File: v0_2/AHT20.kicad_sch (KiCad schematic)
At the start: 1 part, among them U1 AHT20

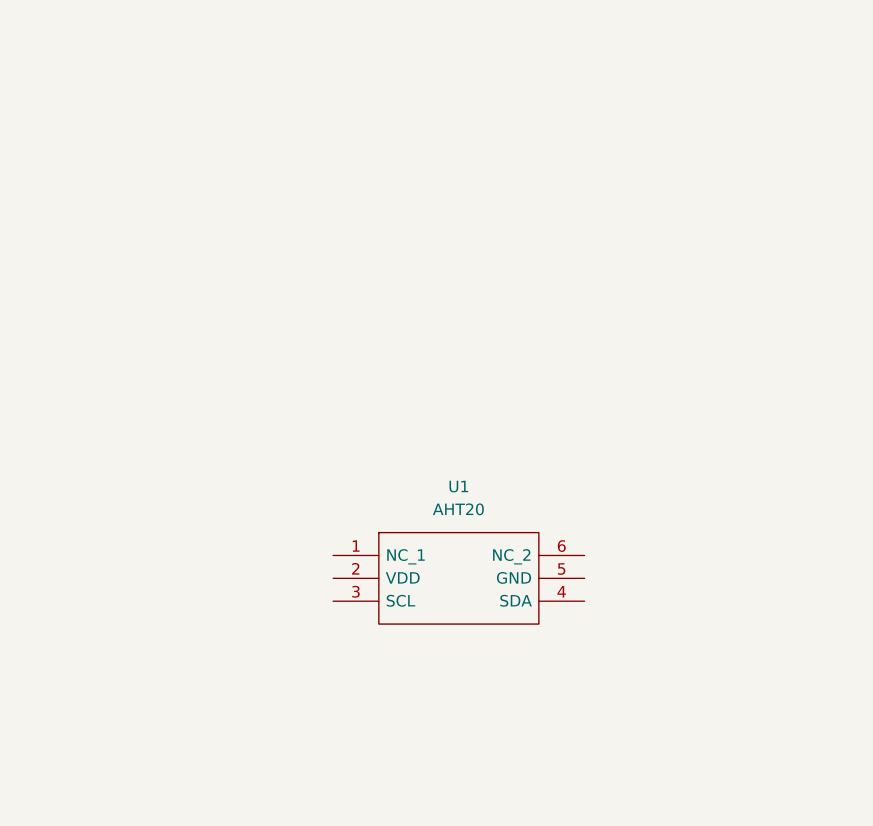
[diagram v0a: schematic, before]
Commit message: add color sensor
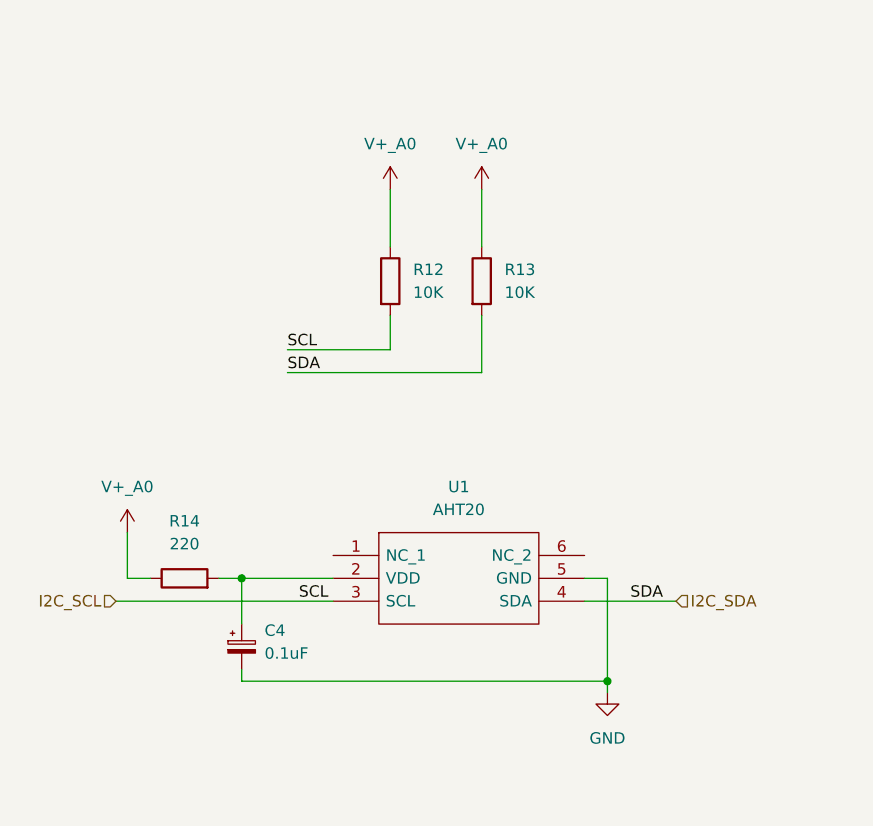
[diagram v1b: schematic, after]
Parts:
- added C4: 0.1uF, symbol Device:C_Polarized_Small
- added R12, R13: 10K, symbol Device:R
- added R14: 220, symbol Device:R
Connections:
- net at U1.2 (VDD): now also C4.1, R14.2
- net I2C_SCL: now reaches U1.3 (SCL)
- net I2C_SCL: now also R12.2
- net I2C_SDA: now reaches U1.4 (SDA)
- net I2C_SDA: now also R13.2
- net GND: now reaches U1.5 (GND)
- net GND: now also C4.2
- new net V+_A0: R12.1, R13.1, R14.1

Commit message: schematic for enviro done
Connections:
- net V+_A0 renamed +3.3V
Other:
- note added: "Temperature / Humidity Sensor"
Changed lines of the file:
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@@
     (stroke (width 0) (type default))
+  )
+  (text "Temperature / Humidity Sensor" (at 93.98 36.83 0)
+    (effects (font (face "Ubuntu") (size 3 3) (thickness 1) bold) (justify left bottom))
   )
   (label "SDA" (at 119.38 71.12 0) (fields_autoplaced)
@@
     )
   )
+  (symbol (lib_id "power:+3.3V") (at 130.81 50.8 0) (unit 1)
+    (in_bom yes) (on_board yes) (dnp no) (fields_autoplaced)
+    (property "Reference" "#PWR018" (at 130.81 54.61 0)
+      (effects (font (size 1.27 1.27)) hide)
+    )
+    (property "Value" "+3.3V" (at 130.81 45.72 0)
+      (effects (font (size 1.27 1.27)))
+    )
+    (property "Footprint" "" (at 130.81 50.8 0)
+      (effects (font (size 1.27 1.27)) hide)
+    )
+    (property "Datasheet" "" (at 130.81 50.8 0)
+      (effects (font (size 1.27 1.27)) hide)
+    )
+    (pin "1")
+    (instances
+      (project "v0_2"
+        (path "/678523e5-508b-4706-b0e0-f17e466a8d09/d7c57ea3-e552-44a2-b229-9294e72b57c9"
+          (reference "#PWR018") (unit 1)
+        )
+      )
+    )
+  )
+  (symbol (lib_id "power:+3.3V") (at 101.6 88.9 0) (unit 1)
+    (in_bom yes) (on_board yes) (dnp no) (fields_autoplaced)
+    (property "Reference" "#PWR022" (at 101.6 92.71 0)
+      (effects (font (size 1.27 1.27)) hide)
+    )
+    (property "Value" "+3.3V" (at 101.6 83.82 0)
+      (effects (font (size 1.27 1.27)))
+    )
+    (property "Footprint" "" (at 101.6 88.9 0)
+      (effects (font (size 1.27 1.27)) hide)
+    )
+    (property "Datasheet" "" (at 101.6 88.9 0)
+      (effects (font (size 1.27 1.27)) hide)
+    )
+    (pin "1")
+    (instances
+      (project "v0_2"
+        (path "/678523e5-508b-4706-b0e0-f17e466a8d09/d7c57ea3-e552-44a2-b229-9294e72b57c9"
+          (reference "#PWR022") (unit 1)
+        )
+      )
+    )
+  )
   (symbol (lib_id "Device:R") (at 130.81 60.96 0) (unit 1)
     (in_bom yes) (on_board yes) (dnp no) (fields_autoplaced)
@@
         (path "/678523e5-508b-4706-b0e0-f17e466a8d09/d7c57ea3-e552-44a2-b229-9294e72b57c9"
           (reference "R12") (unit 1)
-        )
-      )
-    )
-  )
-  (symbol (lib_id "power_vsys:V+_A0") (at 130.81 50.8 0) (unit 1)
-    (in_bom yes) (on_board yes) (dnp no) (fields_autoplaced)
-    (property "Reference" "#PWR09" (at 130.81 54.61 0)
-      (effects (font (size 1.27 1.27)) hide)
-    )
-    (property "Value" "V+_A0" (at 130.81 45.72 0)
-      (effects (font (size 1.27 1.27)))
-    )
-    (property "Footprint" "" (at 130.81 50.8 0)
-      (effects (font (size 1.27 1.27)) hide)
-    )
-    (property "Datasheet" "" (at 130.81 50.8 0)
-      (effects (font (size 1.27 1.27)) hide)
-    )
-    (pin "1")
-    (instances
-      (project "v0_2"
-        (path "/678523e5-508b-4706-b0e0-f17e466a8d09"
-          (reference "#PWR09") (unit 1)
-        )
-        (path "/678523e5-508b-4706-b0e0-f17e466a8d09/d7c57ea3-e552-44a2-b229-9294e72b57c9"
-          (reference "#PWR018") (unit 1)
         )
       )
@@
     )
   )
-  (symbol (lib_id "power_vsys:V+_A0") (at 140.97 50.8 0) (unit 1)
-    (in_bom yes) (on_board yes) (dnp no) (fields_autoplaced)
-    (property "Reference" "#PWR09" (at 140.97 54.61 0)
-      (effects (font (size 1.27 1.27)) hide)
-    )
-    (property "Value" "V+_A0" (at 140.97 45.72 0)
+  (symbol (lib_id "power:+3.3V") (at 140.97 50.8 0) (unit 1)
+    (in_bom yes) (on_board yes) (dnp no) (fields_autoplaced)
+    (property "Reference" "#PWR019" (at 140.97 54.61 0)
+      (effects (font (size 1.27 1.27)) hide)
+    )
+    (property "Value" "+3.3V" (at 140.97 45.72 0)
       (effects (font (size 1.27 1.27)))
     )
@@
     (instances
       (project "v0_2"
-        (path "/678523e5-508b-4706-b0e0-f17e466a8d09"
-          (reference "#PWR09") (unit 1)
-        )
         (path "/678523e5-508b-4706-b0e0-f17e466a8d09/d7c57ea3-e552-44a2-b229-9294e72b57c9"
           (reference "#PWR019") (unit 1)
         )
       )
-    )
-  )
-  (symbol (lib_id "power_vsys:V+_A0") (at 101.6 88.9 0) (unit 1)
-    (in_bom yes) (on_board yes) (dnp no) (fields_autoplaced)
-    (property "Reference" "#PWR09" (at 101.6 92.71 0)
-      (effects (font (size 1.27 1.27)) hide)
-    )
-    (property "Value" "V+_A0" (at 101.6 83.82 0)
-      (effects (font (size 1.27 1.27)))
-    )
-    (property "Footprint" "" (at 101.6 88.9 0)
-      (effects (font (size 1.27 1.27)) hide)
-    )
-    (property "Datasheet" "" (at 101.6 88.9 0)
-      (effects (font (size 1.27 1.27)) hide)
-    )
-    (pin "1")
-    (instances
-      (project "v0_2"
-        (path "/678523e5-508b-4706-b0e0-f17e466a8d09"
-          (reference "#PWR09") (unit 1)
-        )
-        (path "/678523e5-508b-4706-b0e0-f17e466a8d09/d7c57ea3-e552-44a2-b229-9294e72b57c9"
-          (reference "#PWR022") (unit 1)
-        )
-      )

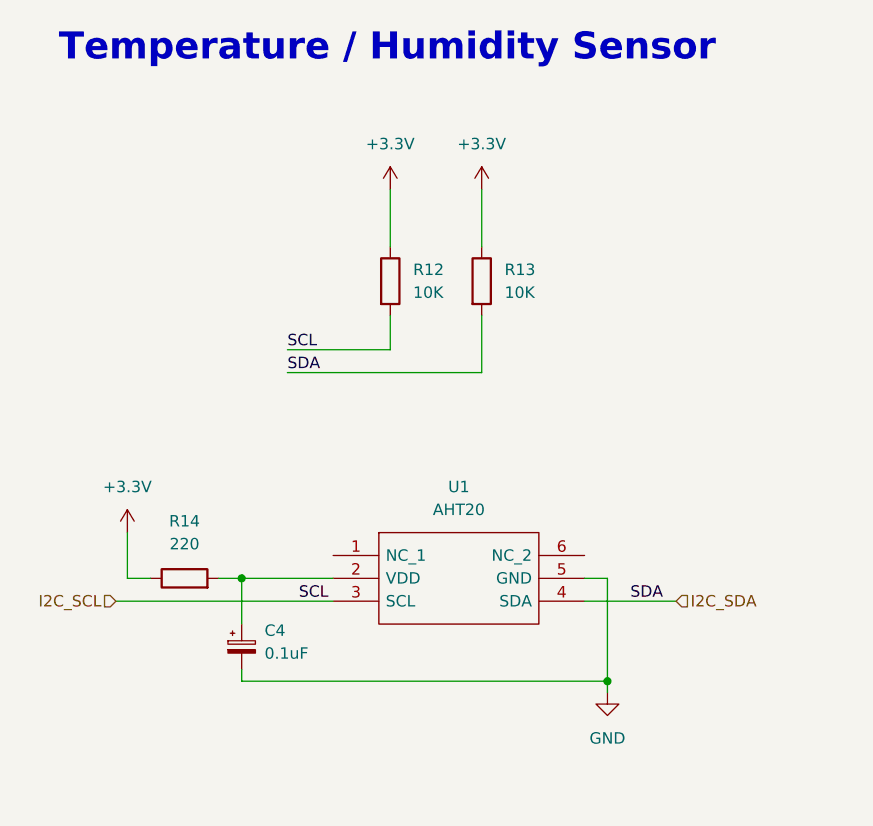
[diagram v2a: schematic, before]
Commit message: all part are added
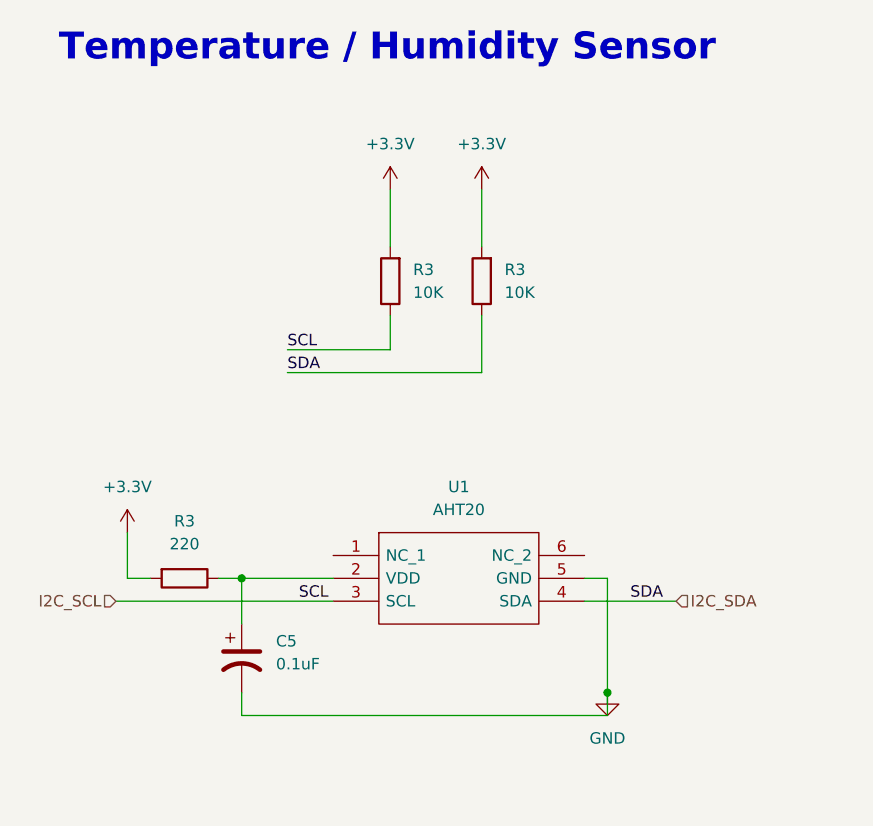
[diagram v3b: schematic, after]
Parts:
- removed C4: 0.1uF, symbol Device:C_Polarized_Small
- removed R12, R13: 10K, symbol Device:R
- removed R14: 220, symbol Device:R
- added C5: 0.1uF, Capacitor_SMD:C_0603_1608Metric, symbol Device:C_Polarized_US
- added R3: 220, Resistor_SMD:R_0603_1608Metric, symbol Device:R
- added R3 (x2): 10K, Resistor_SMD:R_0603_1608Metric, symbol Device:R
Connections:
- net +3.3V: now also R3.2, R3.2, R3.2
- net GND: now also C5.2
- net I2C_SCL: now also R3.1
- net I2C_SDA: now also R3.1
- net at U1.2 (VDD): now also C5.1, R3.1

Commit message: for quoate
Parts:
- removed R3 (x2): 10K, Resistor_SMD:R_0603_1608Metric, symbol Device:R
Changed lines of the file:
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@@
-    (stroke (width 0) (type default))
-  )
-  (wire (pts (xy 140.97 50.8) (xy 140.97 57.15))
     (stroke (width 0) (type default))
   )
@@
     (stroke (width 0) (type default))
   )
-  (wire (pts (xy 119.38 68.58) (xy 130.81 68.58))
-    (stroke (width 0) (type default))
-  )
   (wire (pts (xy 152.4 96.52) (xy 162.56 96.52))
     (stroke (width 0) (type default))
   )
   (wire (pts (xy 100.33 96.52) (xy 124.46 96.52))
-    (stroke (width 0) (type default))
-  )
-  (wire (pts (xy 130.81 68.58) (xy 130.81 64.77))
     (stroke (width 0) (type default))
   )
@@
     (stroke (width 0) (type default))
   )
-  (wire (pts (xy 140.97 71.12) (xy 140.97 64.77))
-    (stroke (width 0) (type default))
-  )
-  (wire (pts (xy 119.38 71.12) (xy 140.97 71.12))
-    (stroke (width 0) (type default))
-  )
-  (wire (pts (xy 130.81 50.8) (xy 130.81 57.15))
-    (stroke (width 0) (type default))
-  )
   (wire (pts (xy 101.6 93.98) (xy 104.14 93.98))
     (stroke (width 0) (type default))
@@
     (effects (font (face "Ubuntu") (size 3 3) (thickness 1) bold) (justify left bottom))
   )
-  (label "SDA" (at 119.38 71.12 0) (fields_autoplaced)
-    (effects (font (size 1.27 1.27)) (justify left bottom))
-  )
   (label "SCL" (at 120.65 96.52 0) (fields_autoplaced)
     (effects (font (size 1.27 1.27)) (justify left bottom))
   )
   (label "SDA" (at 157.48 96.52 0) (fields_autoplaced)
-    (effects (font (size 1.27 1.27)) (justify left bottom))
-  )
-  (label "SCL" (at 119.38 68.58 0) (fields_autoplaced)
     (effects (font (size 1.27 1.27)) (justify left bottom))
   )
@@
         (path "/678523e5-508b-4706-b0e0-f17e466a8d09/d7c57ea3-e552-44a2-b229-9294e72b57c9"
           (reference "R12") (unit 1)
-        )
-      )
-    )
-  )
-  (symbol (lib_id "power:+3.3V") (at 130.81 50.8 0) (unit 1)
-    (in_bom yes) (on_board yes) (dnp no) (fields_autoplaced)
-    (property "Reference" "#PWR018" (at 130.81 54.61 0)
-      (effects (font (size 1.27 1.27)) hide)
-    )
-    (property "Value" "+3.3V" (at 130.81 45.72 0)
-      (effects (font (size 1.27 1.27)))
-    )
-    (property "Footprint" "" (at 130.81 50.8 0)
-      (effects (font (size 1.27 1.27)) hide)
-    )
-    (property "Datasheet" "" (at 130.81 50.8 0)
-      (effects (font (size 1.27 1.27)) hide)
-    )
-    (pin "1")
-    (instances
-      (project "v0_2"
-        (path "/678523e5-508b-4706-b0e0-f17e466a8d09/d7c57ea3-e552-44a2-b229-9294e72b57c9"
-          (reference "#PWR018") (unit 1)
-        )
-      )
-    )
-  )
-  (symbol (lib_id "Device:R") (at 140.97 60.96 180) (unit 1)
-    (in_bom yes) (on_board yes) (dnp no) (fields_autoplaced)
-    (property "Reference" "R3" (at 143.51 59.69 0)
-      (effects (font (size 1.27 1.27)) (justify right))
-    )
-    (property "Value" "10K" (at 143.51 62.23 0)
-      (effects (font (size 1.27 1.27)) (justify right))
-    )
-    (property "Footprint" "Resistor_SMD:R_0603_1608Metric" (at 142.748 60.96 90)
-      (effects (font (size 1.27 1.27)) hide)
-    )
-    (property "Datasheet" "~" (at 140.97 60.96 0)
-      (effects (font (size 1.27 1.27)) hide)
-    )
-    (property "Manufacturer_Part_Number" "0603WAF1002T5E" (at 140.97 60.96 90)
-      (effects (font (size 1.27 1.27)) hide)
-    )
-    (pin "1")
-    (pin "2")
-    (instances
-      (project "v0_2"
-        (path "/678523e5-508b-4706-b0e0-f17e466a8d09"
-          (reference "R3") (unit 1)
-        )
-        (path "/678523e5-508b-4706-b0e0-f17e466a8d09/d7c57ea3-e552-44a2-b229-9294e72b57c9"
-          (reference "R18") (unit 1)
         )
       )
@@
         )
       )
-    )
-  )
-  (symbol (lib_id "power:+3.3V") (at 140.97 50.8 0) (unit 1)
-    (in_bom yes) (on_board yes) (dnp no) (fields_autoplaced)
-    (property "Reference" "#PWR019" (at 140.97 54.61 0)
-      (effects (font (size 1.27 1.27)) hide)
-    )
-    (property "Value" "+3.3V" (at 140.97 45.72 0)
-      (effects (font (size 1.27 1.27)))
-    )
-    (property "Footprint" "" (at 140.97 50.8 0)
-      (effects (font (size 1.27 1.27)) hide)
-    )
-    (property "Datasheet" "" (at 140.97 50.8 0)
-      (effects (font (size 1.27 1.27)) hide)
-    )
-    (pin "1")
-    (instances
-      (project "v0_2"
-        (path "/678523e5-508b-4706-b0e0-f17e466a8d09/d7c57ea3-e552-44a2-b229-9294e72b57c9"
-          (reference "#PWR019") (unit 1)
-        )
-      )
-    )
-  )
-  (symbol (lib_id "Device:R") (at 130.81 60.96 180) (unit 1)
-    (in_bom yes) (on_board yes) (dnp no) (fields_autoplaced)
-    (property "Reference" "R3" (at 133.35 59.69 0)
-      (effects (font (size 1.27 1.27)) (justify right))
-    )
-    (property "Value" "10K" (at 133.35 62.23 0)
-      (effects (font (size 1.27 1.27)) (justify right))
-    )
-    (property "Footprint" "Resistor_SMD:R_0603_1608Metric" (at 132.588 60.96 90)
-      (effects (font (size 1.27 1.27)) hide)
-    )
-    (property "Datasheet" "~" (at 130.81 60.96 0)
-      (effects (font (size 1.27 1.27)) hide)
-    )
-    (property "Manufacturer_Part_Number" "0603WAF1002T5E" (at 130.81 60.96 90)
-      (effects (font (size 1.27 1.27)) hide)
-    )
-    (pin "1")
-    (pin "2")
-    (instances
-      (project "v0_2"
-        (path "/678523e5-508b-4706-b0e0-f17e466a8d09"
-          (reference "R3") (unit 1)
-        )
-        (path "/678523e5-508b-4706-b0e0-f17e466a8d09/d7c57ea3-e552-44a2-b229-9294e72b57c9"
-          (reference "R6") (unit 1)
-        )
-      )

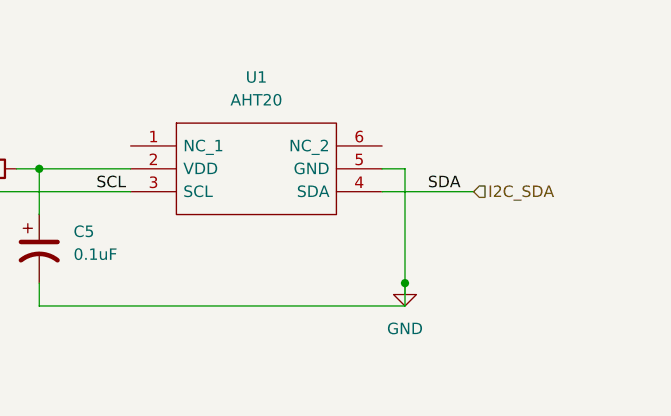
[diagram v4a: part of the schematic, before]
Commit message: rename i2c and add button
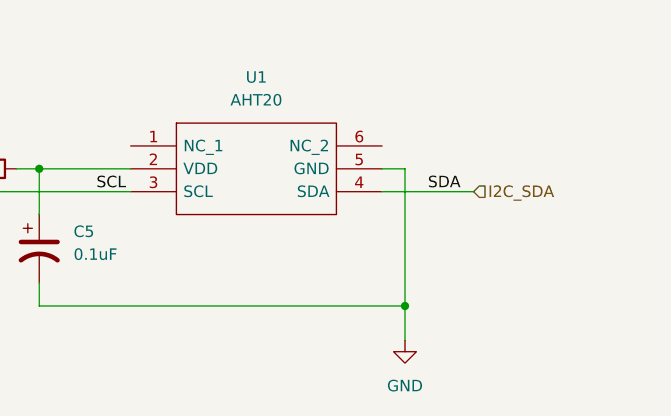
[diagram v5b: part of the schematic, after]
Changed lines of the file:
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@@
   (junction (at 114.3 93.98) (diameter 0) (color 0 0 0 0)
   )
-  (junction (at 154.94 106.68) (diameter 0) (color 0 0 0 0)
+  (junction (at 154.94 109.22) (diameter 0) (color 0 0 0 0)
   )
   (wire (pts (xy 114.3 93.98) (xy 114.3 99.06))
@@
     (stroke (width 0) (type default))
   )
-  (wire (pts (xy 154.94 93.98) (xy 154.94 106.68))
+  (wire (pts (xy 154.94 93.98) (xy 154.94 109.22))
     (stroke (width 0) (type default))
   )
@@
     (stroke (width 0) (type default))
   )
-  (wire (pts (xy 154.94 109.22) (xy 154.94 106.68))
+  (wire (pts (xy 154.94 113.03) (xy 154.94 109.22))
     (stroke (width 0) (type default))
   )
@@
     )
   )
-  (symbol (lib_id "power:GND") (at 154.94 106.68 0) (unit 1)
-    (in_bom yes) (on_board yes) (dnp no) (fields_autoplaced)
-    (property "Reference" "#PWR023" (at 154.94 113.03 0)
-      (effects (font (size 1.27 1.27)) hide)
-    )
-    (property "Value" "GND" (at 154.94 111.76 0)
-      (effects (font (size 1.27 1.27)))
-    )
-    (property "Footprint" "" (at 154.94 106.68 0)
-      (effects (font (size 1.27 1.27)) hide)
-    )
-    (property "Datasheet" "" (at 154.94 106.68 0)
-      (effects (font (size 1.27 1.27)) hide)
-    )
+  (symbol (lib_id "power:GND") (at 154.94 113.03 0) (unit 1)
+    (in_bom yes) (on_board yes) (dnp no) (fields_autoplaced)
+    (property "Reference" "#PWR023" (at 154.94 119.38 0)
+      (effects (font (size 1.27 1.27)) hide)
+    )
+    (property "Value" "GND" (at 154.94 118.11 0)
+      (effects (font (size 1.27 1.27)))
+    )
+    (property "Footprint" "" (at 154.94 113.03 0)
+      (effects (font (size 1.27 1.27)) hide)
+    )
+    (property "Datasheet" "" (at 154.94 113.03 0)
+      (effects (font (size 1.27 1.27)) hide)
+    )
